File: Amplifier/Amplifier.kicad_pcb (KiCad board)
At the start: 2 copper layers, 77.7 x 60 mm, 39 parts, among them J1 Screw_Terminal_01x02, J3 Screw_Terminal_01x02, U1 PA88

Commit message: update
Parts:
- added JP1: Jumper_2_Open, Jumper:SolderJumper-2_P1.3mm_Open_RoundedPad1.0x1.5mm, B.Cu at (185.1, 97.4)
- added R14: 68k, Resistor_SMD:R_1206_3216Metric_Pad1.30x1.75mm_HandSolder, F.Cu at (183.2, 64.4)
- added R15: 68k, Resistor_SMD:R_1206_3216Metric_Pad1.30x1.75mm_HandSolder, F.Cu at (180.4, 93.1)
- added R7: 100, Resistor_SMD:R_1206_3216Metric_Pad1.30x1.75mm_HandSolder, B.Cu at (185.0, 100.0)
- D5, D6: value D_Zener 6.1V -> D_Zener 6.2V
- R11, R12, R8: value 110K -> 68k
- R4, R5: moved to F.Cu
- R6: value 100 -> 11; moved to F.Cu
- R9: value 110K -> 68K
- RV1: value 200 -> 100
- moved R12 15.6 mm to (192.1, 77.5), turned to 90 degrees
- moved J1 5.85 mm to (162.2, 107.8)
- moved R6 5.60 mm to (163.8, 95.2)
- moved R4 3.61 mm to (172.0, 100.0)
- moved C2 1.77 mm to (200.7, 93.8)
- moved C5 1.24 mm to (192.7, 88.5)
- moved C20 1.17 mm to (144.9, 68.9), turned to -135 degrees
- moved R8 1.16 mm to (184.6, 94.4)
- moved R5 1.11 mm to (166.6, 100.0)
- moved D6 1.02 mm to (198.0, 93.8)
- moved D5 0.88 mm to (190.2, 88.3)
- renumbered R17 to Termination
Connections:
- H3 pad 1: unconnected-(H3-Pad1) -> GND
- H4 pad 1: GND -> unconnected-(H4-Pad1)
- R12 pad 2: Net-(R11-Pad1) -> Net-(R12-Pad2)
- R2 pad 2: GND -> Net-(JP1-B)
- R8 pad 2: +VHV -> Net-(R15-Pad1)
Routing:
- net -VLV: track 41.2 -> 20.4 mm, vias 2 -> 0
- net Net-(R12-Pad2): track 0.00 -> 14.7 mm
- net Net-(JP1-B): track 0.00 -> 5.67 mm
- net Net-(U1-CL): track 4.27 -> 9.91 mm
- net Net-(R15-Pad1): track 0.00 -> 2.76 mm
- net +VHV: track 64.2 -> 61.6 mm
- net /HVOUT: track 28.5 -> 31.1 mm, vias 1 -> 0
- net GND: track 22.4 -> 20.6 mm
- net Net-(R4-Pad1): track 3.71 -> 2.36 mm
- net +VLV: track 10.7 -> 9.41 mm
- net Net-(D1-A): track 35.8 -> 34.8 mm
- net -VHV: track 62.0 -> 61.0 mm
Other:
- board text added: "Danger! High Voltage +-200v"
- board text added: "I set"

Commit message: update
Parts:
- removed JP1: Jumper_2_Open, Jumper:SolderJumper-2_P1.3mm_Open_RoundedPad1.0x1.5mm
- R3: value 10M -> 330k
- R4, R5: value 49.9K -> 50K
- R7: value 100 -> 160
- RV1: value 100 -> 10
- moved R5 2.72 mm to (163.9, 100.0)
- moved R3 2.17 mm to (179.2, 108.7)
- moved R4 0.13 mm to (171.9, 100.0)
- renumbered Termination to R17
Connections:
- H1 pad 1: unconnected-(H1-Pad1) -> GND
- R2 pad 2: Net-(JP1-B) -> Net-(R2-Pad2)
- R3 pad 1: Net-(R2-Pad1) -> Net-(R2-Pad2)
- R7 pad 1: Net-(JP1-B) -> Net-(R2-Pad2)
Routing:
- net Net-(R2-Pad2): track 0.00 -> 10.5 mm
- net /HVOUT: track 31.1 -> 25.1 mm
- net Net-(JP1-B): track 5.67 -> 0.00 mm
- net Net-(D1-A): track 34.8 -> 39.0 mm
- net Net-(R4-Pad1): track 2.36 -> 4.98 mm
- net Net-(R3-Pad2): track 4.47 -> 5.39 mm
- added copper zone on F.Cu, net Net-(R4-Pad1)

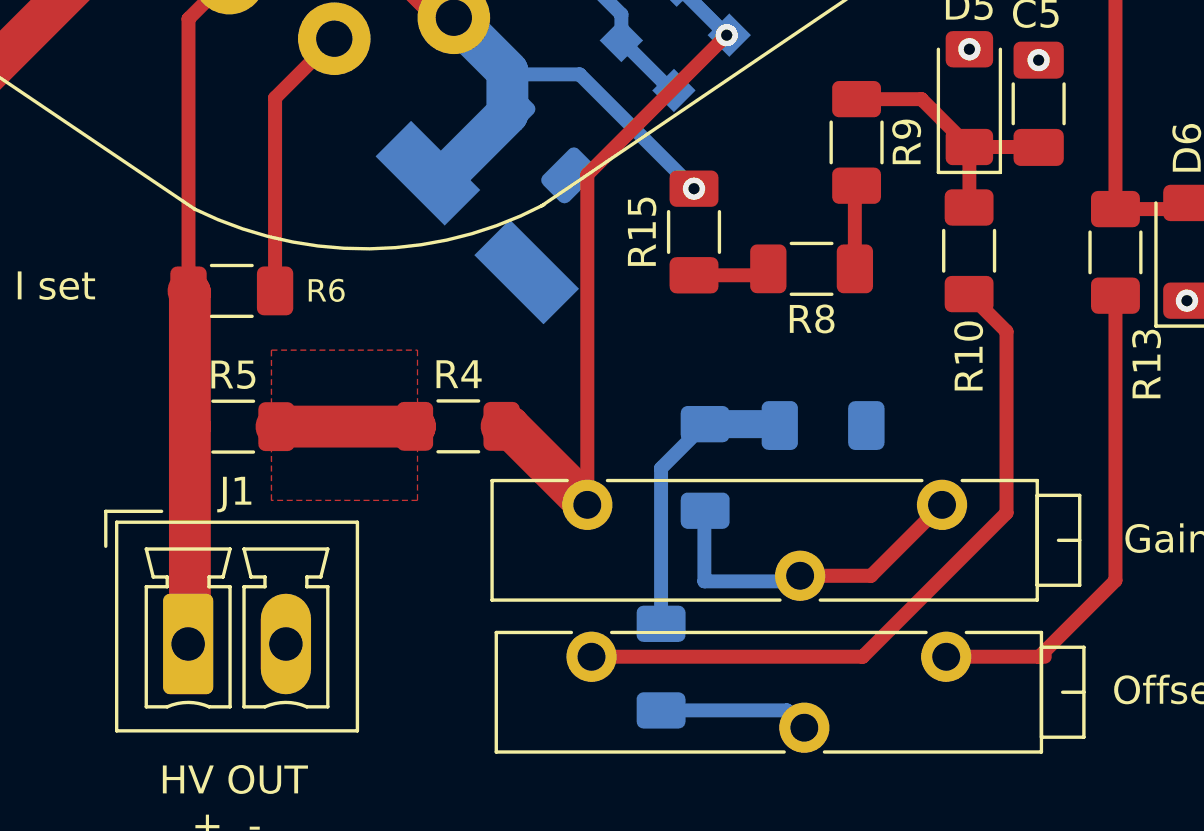
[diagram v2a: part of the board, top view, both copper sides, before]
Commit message: update feedback resistor to 200k
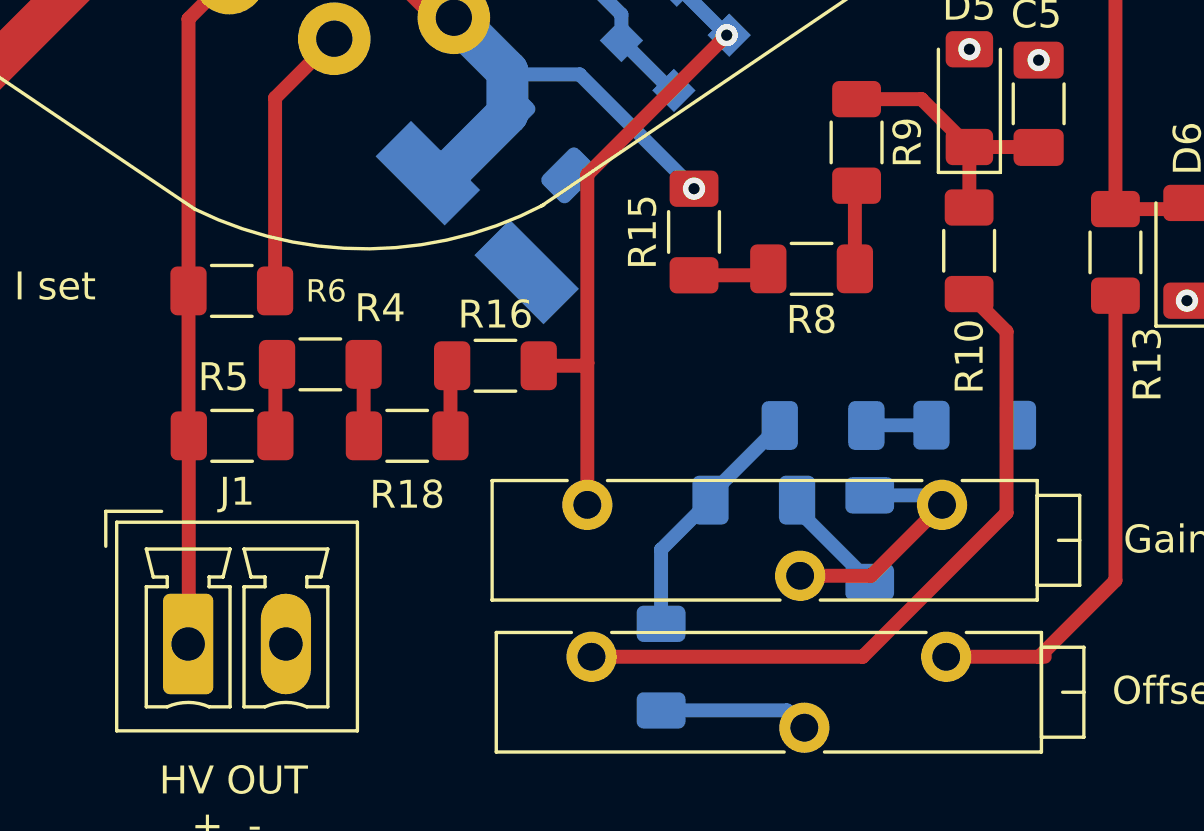
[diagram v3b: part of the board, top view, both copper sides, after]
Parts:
- added R16: 50K, Resistor_SMD:R_1206_3216Metric_Pad1.30x1.75mm_HandSolder, F.Cu at (173.2, 97.9)
- added R18: 50K, Resistor_SMD:R_1206_3216Metric_Pad1.30x1.75mm_HandSolder, F.Cu at (170.1, 100.4)
- added R19: 5.1K, Resistor_SMD:R_1206_3216Metric_Pad1.30x1.75mm_HandSolder, B.Cu at (186.7, 104.1)
- added R20: 160, Resistor_SMD:R_1206_3216Metric_Pad1.30x1.75mm_HandSolder, B.Cu at (190.4, 100.0)
- moved R4 5.42 mm to (167.0, 97.8)
- moved R2 2.10 mm to (182.5, 102.7), turned to 180 degrees
- moved R5 0.33 mm to (163.8, 100.4)
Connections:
- R2 pad 1: Net-(R2-Pad1) -> Net-(R19-Pad2)
- R4 pad 2: Net-(D1-A) -> Net-(R18-Pad1)
- R7 pad 2: GND -> Net-(R20-Pad1)
- RV1 pad 2: Net-(R2-Pad1) -> Net-(R19-Pad1)
- RV1 pad 3: Net-(R2-Pad1) -> Net-(R19-Pad1)
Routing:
- net Net-(R2-Pad1): track 12.2 -> 0.00 mm
- net Net-(R19-Pad1): track 0.00 -> 9.37 mm
- net Net-(D1-A): track 39.0 -> 32.4 mm
- net Net-(R19-Pad2): track 0.00 -> 4.01 mm
- net Net-(R18-Pad1): track 0.00 -> 2.56 mm
- net Net-(R16-Pad1): track 0.00 -> 2.53 mm
- net Net-(R4-Pad1): track 4.98 -> 2.58 mm
- net Net-(R20-Pad1): track 0.00 -> 2.33 mm
- net Net-(R2-Pad2): track 10.5 -> 8.93 mm
- net /HVOUT: track 25.1 -> 24.5 mm
- removed copper zone on F.Cu, net Net-(R4-Pad1)
